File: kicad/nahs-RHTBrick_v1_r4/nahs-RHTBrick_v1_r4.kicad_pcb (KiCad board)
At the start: 2 copper layers, 45 x 70 mm, 70 parts, among them IC1 ESP12S, J2 USB_B_Mini, Q1 8205A, Q2 AP2301B, Q3 CJ2302, Q4 MMBT2907A, SW1 KMR_231_G_LFS, SW2 SSSS820101, U1 ZD8028IB5TR, U2 HDC1080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

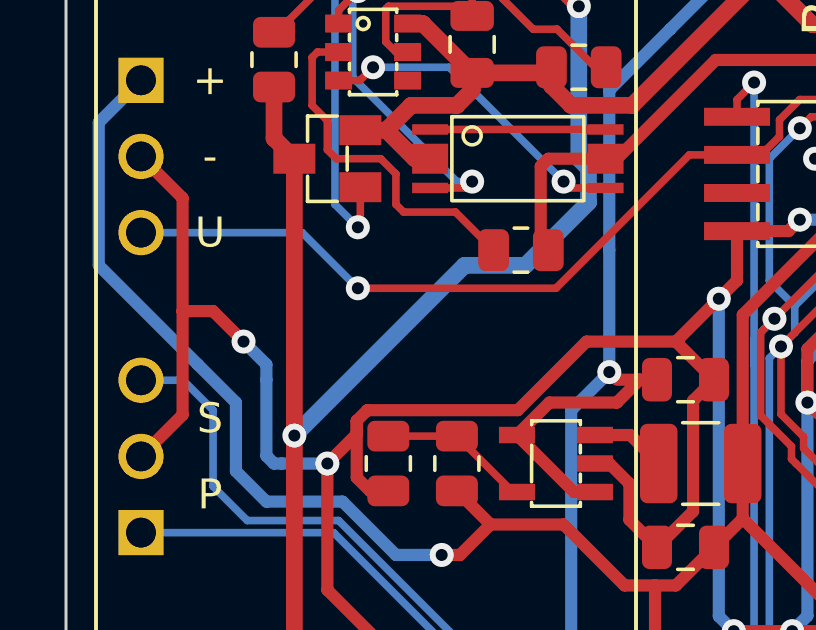
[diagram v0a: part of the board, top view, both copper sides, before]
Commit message: added forgotten logo on v1.0 R4 Board
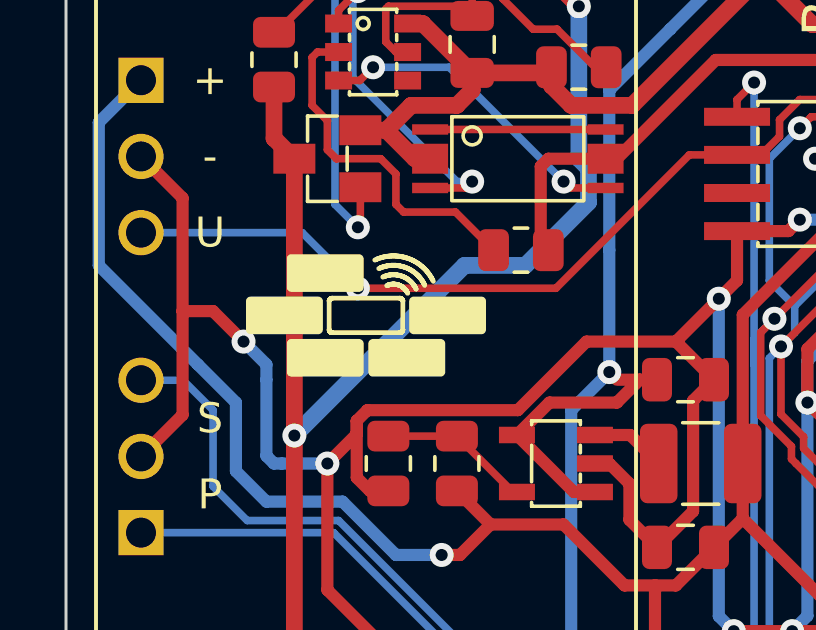
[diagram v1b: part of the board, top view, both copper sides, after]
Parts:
- added LOGOF: x8mm, no_brick_logo:x8mm, F.Cu at (110.0, 105.3)
- renumbered LOGO to LOGOB
